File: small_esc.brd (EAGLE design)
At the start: 100 x 80 mm, 46 parts, among them Q1 MOSFET-PCHANNELDPAKK, Q2 MOSFET-NCHANNELFDD8780, Q3 200mA/50V, Q4 MOSFET-PCHANNELDPAKK, Q5 MOSFET-NCHANNELFDD8780, Q6 200mA/50V, Q7 MOSFET-PCHANNELDPAKK, Q8 MOSFET-NCHANNELFDD8780, Q9 200mA/50V

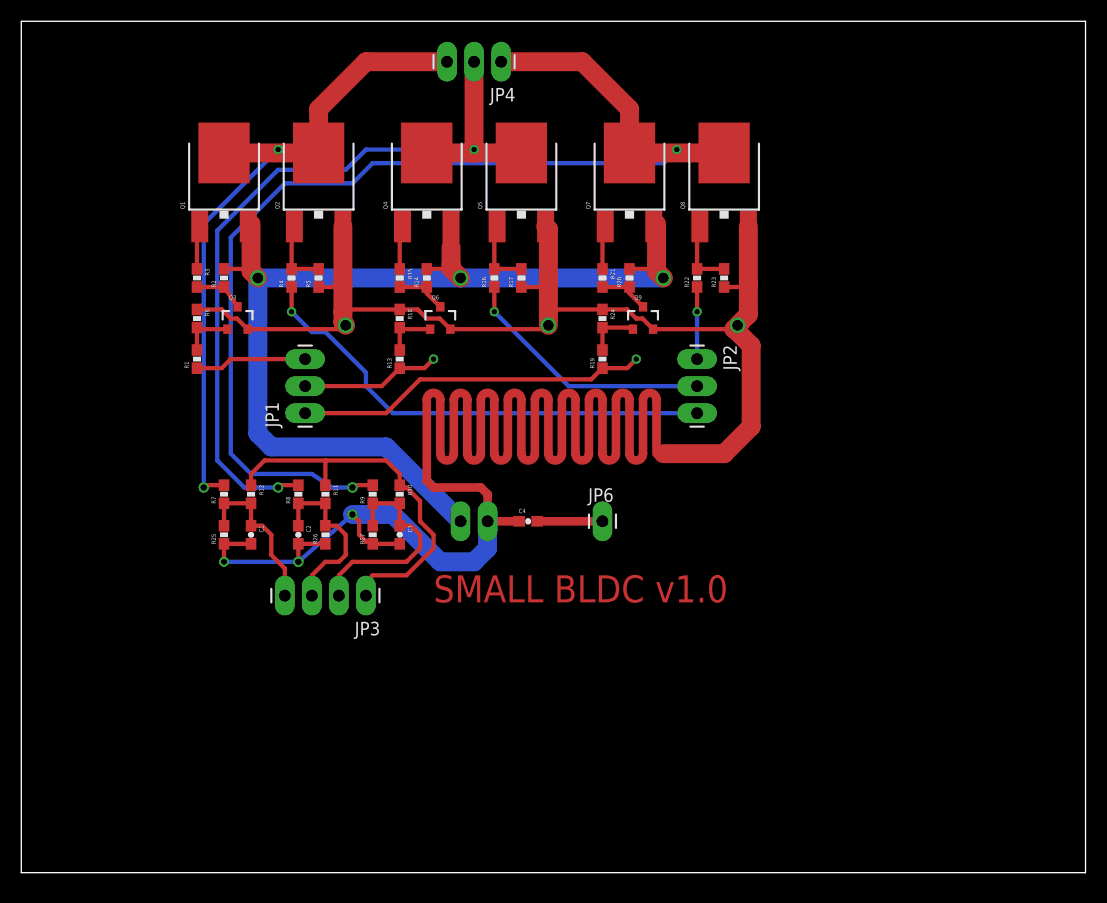
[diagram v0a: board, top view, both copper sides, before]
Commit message: add bypass capacitors
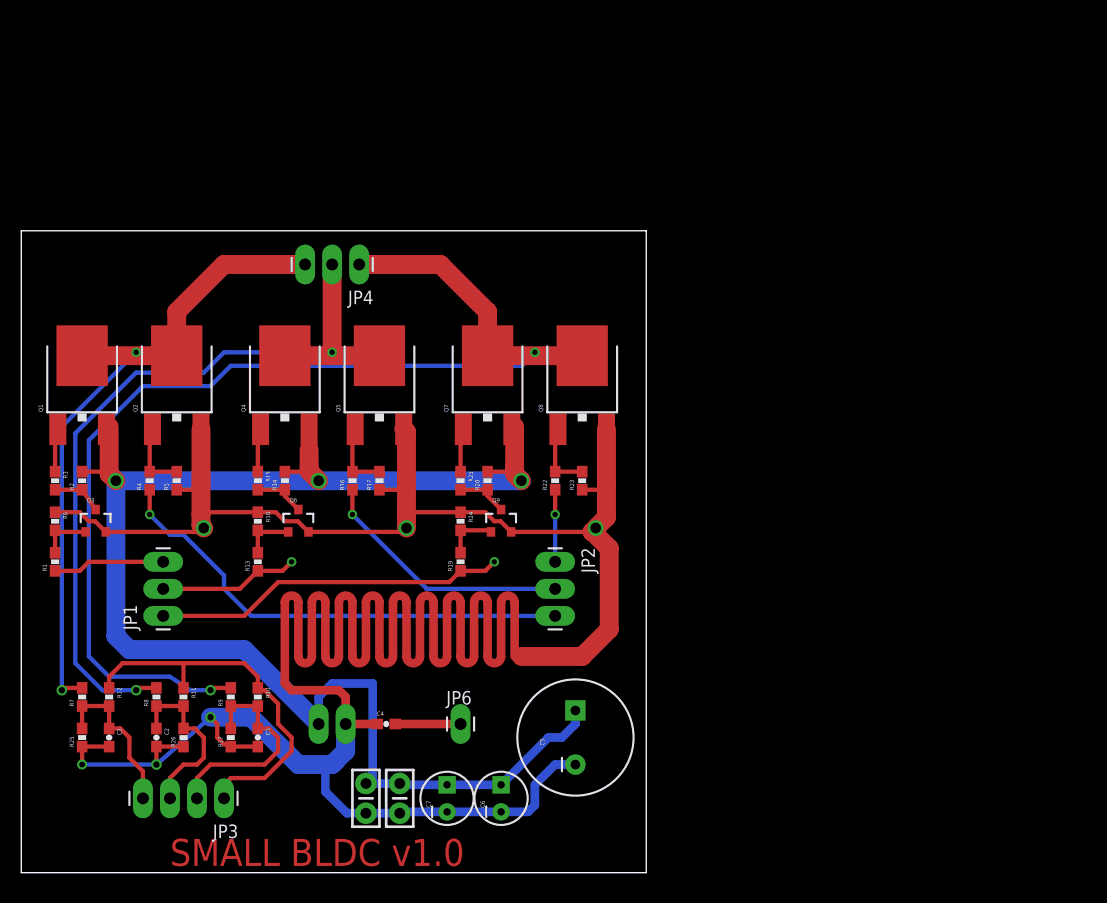
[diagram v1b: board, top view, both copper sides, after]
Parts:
- added C5: CAP-09538, SparkFun-Capacitors:CPOL-RADIAL-1000UF-25V
- added C6, C7: (no value), SparkFun-Capacitors:CPOL-RADIAL-10UF-25V
- added C8, C9: (no value), SparkFun-Capacitors:CAP-PTH-SMALL-KIT
- moved Q8 23.3 mm to (52.7, 47.0)
- moved R23 23.3 mm to (52.7, 36.8)
- moved C4 23.3 mm to (34.3, 14.0)
- moved JP4 23.3 mm to (31.8, 57.1)
- moved JP6 23.3 mm to (41.3, 14.0)
- moved Q1 23.3 mm to (5.71, 47.0)
- moved Q2 23.3 mm to (14.6, 47.0)
- moved Q4 23.3 mm to (24.8, 47.0)
- moved Q5 23.3 mm to (33.7, 47.0)
- moved Q7 23.3 mm to (43.8, 47.0)
- moved R14 23.3 mm to (24.8, 36.8)
- moved R15 23.3 mm to (22.2, 36.8)
- moved R16 23.3 mm to (31.1, 36.8)
- moved R17 23.3 mm to (33.7, 36.8)
- moved R2 23.3 mm to (5.71, 36.8)
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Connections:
- net GND: now also C5.-, C6.2, C7.2, C8.2, C9.2
- net VCC: now also C5.+, C6.1, C7.1, C8.1, C9.1
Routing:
- net VCC: track 99.1 -> 140.3 mm
- net GND: track 288.8 -> 321.4 mm
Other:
- board size 100 x 80 mm -> 58.7 x 60.3 mm
